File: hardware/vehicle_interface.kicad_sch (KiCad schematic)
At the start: 3 parts, among them J2 FCR7350, J3 FCR7350, J4 FCR7350

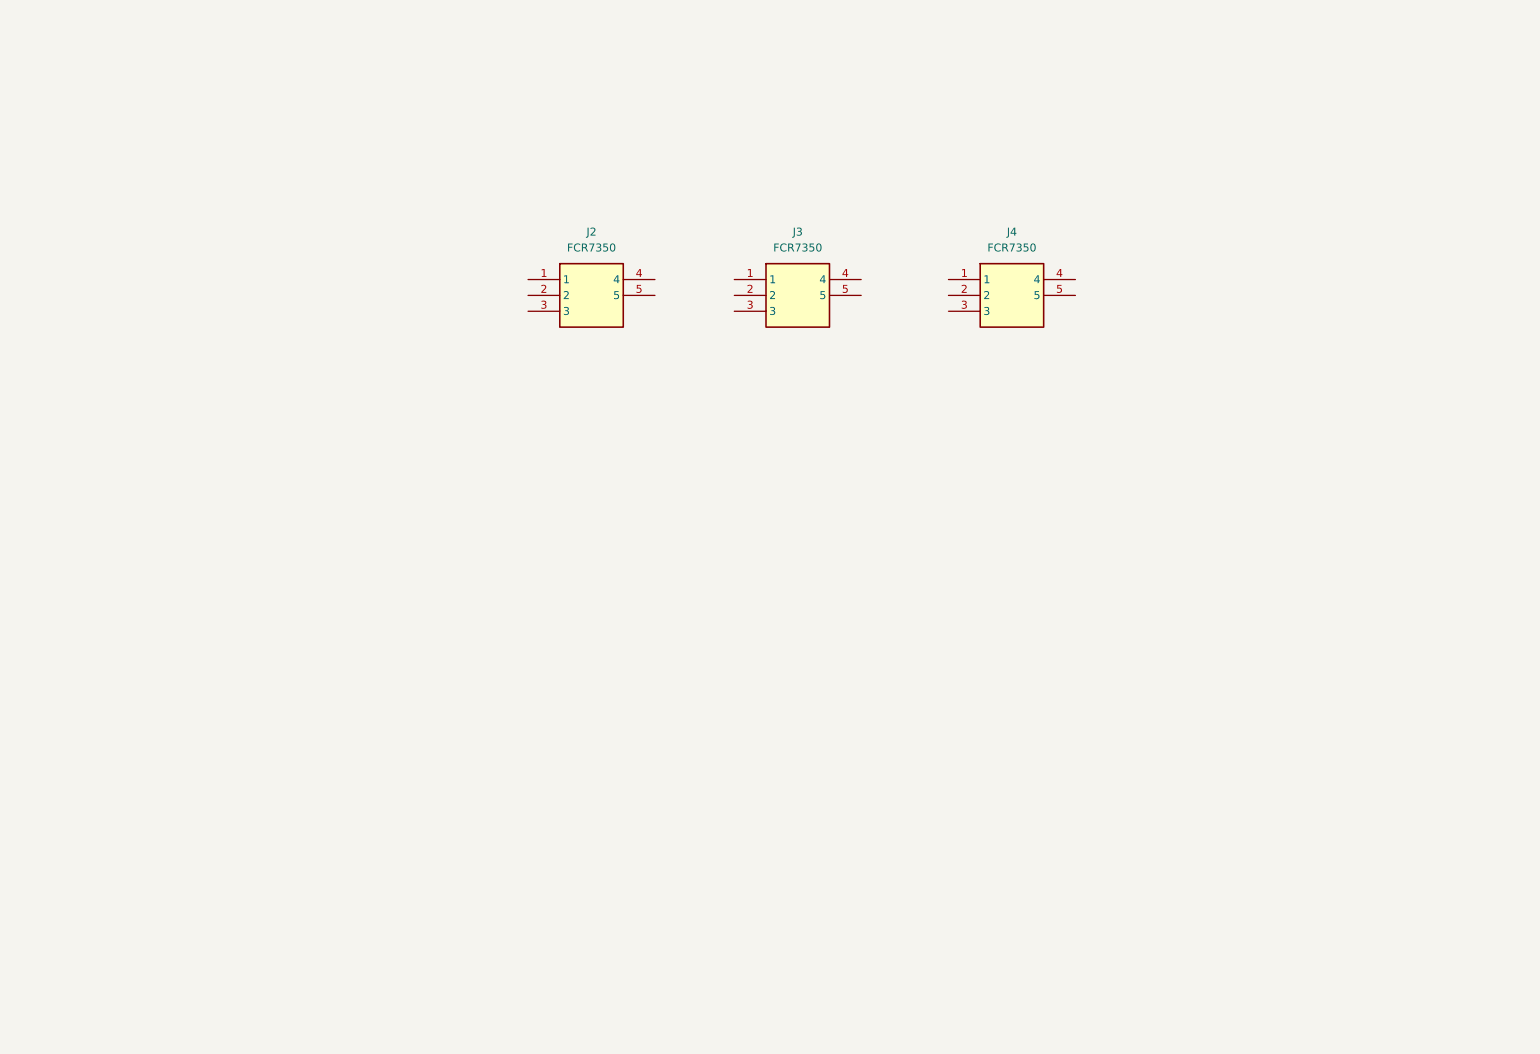
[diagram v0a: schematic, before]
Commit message: CAN ADC on the board
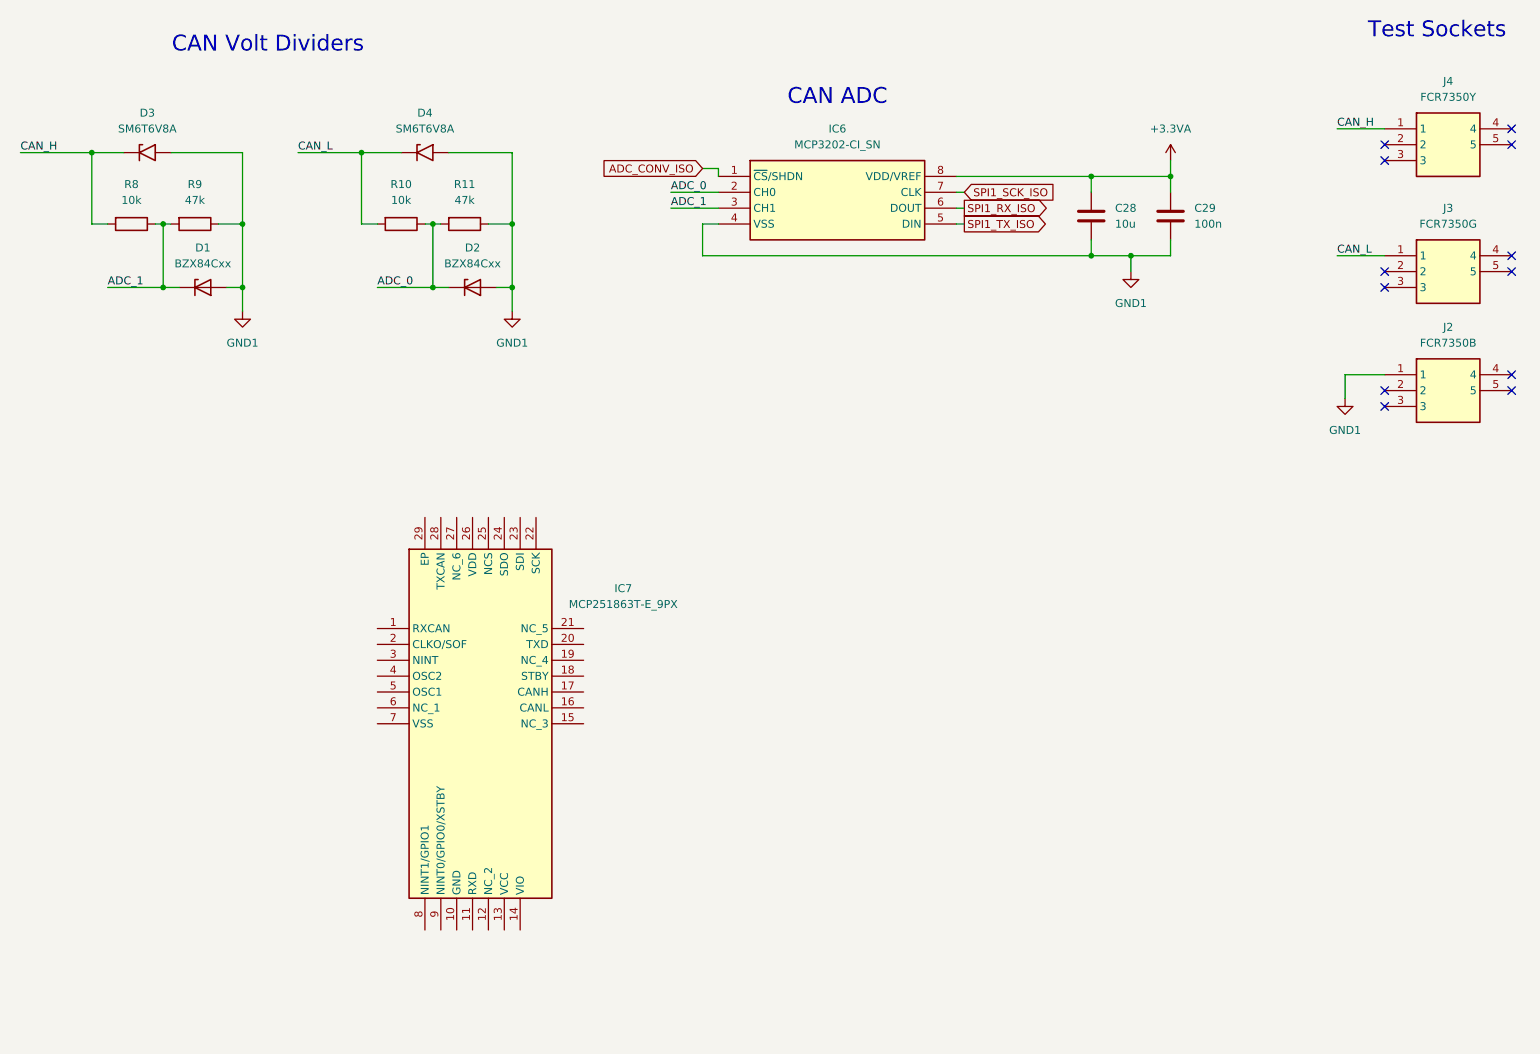
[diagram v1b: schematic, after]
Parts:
- added C28: 10u, Capacitor_SMD:C_0603_1608Metric, symbol Device:C
- added C29: 100n, Capacitor_SMD:C_0402_1005Metric, symbol Device:C
- added D1, D2: BZX84Cxx, Package_TO_SOT_SMD:SOT-23, symbol Diode:BZX84Cxx
- added D3, D4: SM6T6V8A, Diode_SMD:D_SMB, symbol Diode:SM6T6V8A
- added IC6: MCP3202-CI_SN, Stuttgart:SOIC127P600X175-8N, symbol Stuttgart:MCP3202-CI_SN
- added IC7: MCP251863T-E_9PX, Stuttgart:QFN50P500X500X90-29N-D, symbol Stuttgart:MCP251863T-E_9PX
- added R10, R8: 10k, Resistor_SMD:R_0402_1005Metric, symbol Device:R
- added R11, R9: 47k, Resistor_SMD:R_0402_1005Metric, symbol Device:R
- J2: value FCR7350 -> FCR7350B
- J3: value FCR7350 -> FCR7350G
- J4: value FCR7350 -> FCR7350Y
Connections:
- net CAN_H: now reaches J4.1
- net CAN_H: now also D3.1 (A1), R8.2
- net CAN_L: now reaches J3.1
- net CAN_L: now also D4.1 (A1), R10.2
- net GND1: now reaches J2.1
- net GND1: now also C28.2, C29.2, D1.1 (A), D2.1 (A), D3.2 (A2), D4.2 (A2), IC6.4 (VSS), R11.1, R9.1
- new net +3.3VA: C28.1, C29.1, IC6.8 (VDD/VREF)
- new net ADC_0: D2.3 (K), IC6.2 (CH0), R10.1, R11.2
- new net ADC_1: D1.3 (K), IC6.3 (CH1), R8.1, R9.2
- new net ADC_CONV_ISO: IC6.1 (~{CS}/SHDN)
- new net SPI1_RX_ISO: IC6.6 (DOUT)
- new net SPI1_SCK_ISO: IC6.7 (CLK)
- new net SPI1_TX_ISO: IC6.5 (DIN)
- no-connect marks 0 -> 12
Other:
- note added: "CAN ADC"
- note added: "CAN Volt Dividers"
- note added: "Test Sockets"
- moved on the sheet: J2, J3, J4

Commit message: Further CAN IC work before reworking SPI bridges
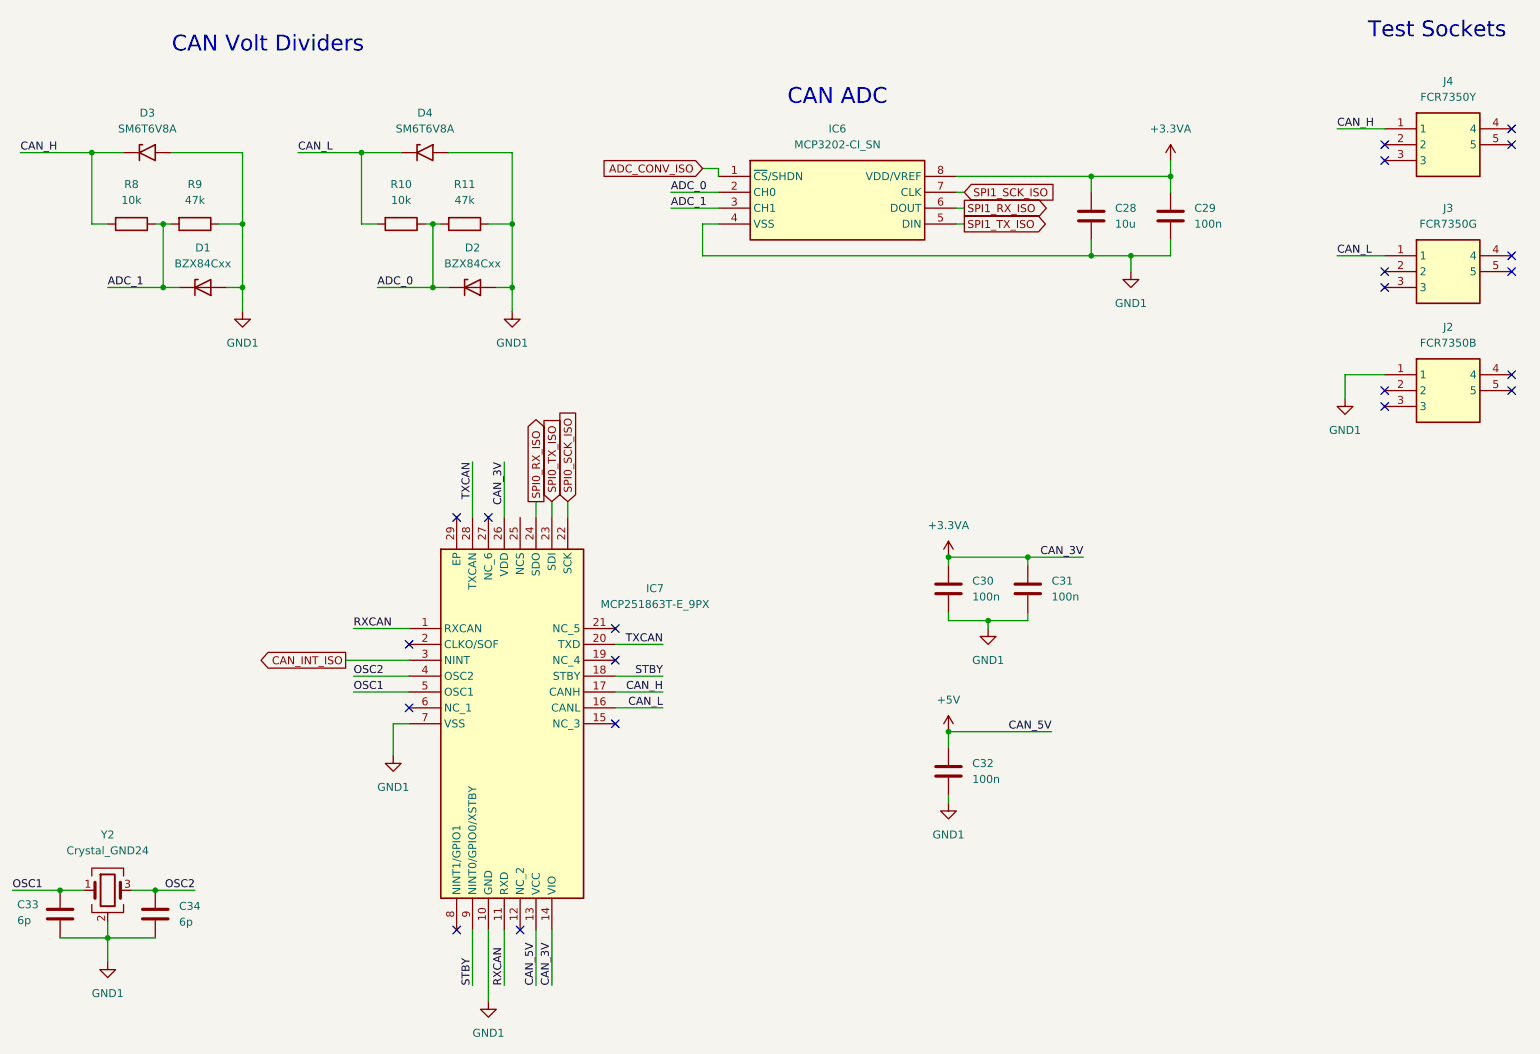
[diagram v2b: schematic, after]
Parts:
- added C30, C31, C32: 100n, Capacitor_SMD:C_0402_1005Metric, symbol Device:C
- added C33, C34: 6p, Capacitor_SMD:C_0402_1005Metric, symbol Device:C
- added Y2: Crystal_GND24, Crystal:Crystal_SMD_2016-4Pin_2.0x1.6mm, symbol Device:Crystal_GND24
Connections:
- net +3.3VA: now also IC7.14 (VIO), IC7.26 (VDD), C30.1, C31.1
- net CAN_H: now also IC7.17 (CANH)
- net CAN_L: now also IC7.16 (CANL)
- net GND1: now also IC7.10 (GND), IC7.7 (VSS), C30.2, C31.2, C32.2, C33.2, C34.2, Y2.2 (G), Y2.4 (G)
- net RXCAN: now reaches IC7.1 (RXCAN)
- net RXCAN: now also IC7.11 (RXD)
- net +5V: now reaches IC7.13 (VCC)
- net +5V: now also C32.1
- net STBY: now reaches IC7.18 (STBY)
- net STBY: now also IC7.9 (NINT0/GPIO0/XSTBY)
- net TXCAN: now reaches IC7.20 (TXD)
- net TXCAN: now also IC7.28 (TXCAN)
- net SPI0_SCK_ISO: now reaches IC7.22 (SCK)
- net SPI0_TX_ISO: now reaches IC7.23 (SDI)
- net SPI0_RX_ISO: now reaches IC7.24 (SDO)
- net CAN_INT_ISO: now reaches IC7.3 (NINT)
- net OSC2: now reaches IC7.4 (OSC2)
- net OSC2: now also C34.1, Y2.3
- net OSC1: now reaches IC7.5 (OSC1)
- net OSC1: now also C33.1, Y2.1
- no-connect marks 12 -> 21
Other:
- moved on the sheet: IC7

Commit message: Further iso bridge development
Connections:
- net SPI0_CS_ISO: now reaches IC7.25 (NCS)
- net CAN_INT1_ISO: now reaches IC7.8 (NINT1/GPIO1)
- net ADC_CONV_ISO renamed SPI1_CS_ISO
- no-connect marks 21 -> 20
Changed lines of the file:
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@@
-	)
-	(no_connect
-		(at 99.06 168.91)
 	)
 	(no_connect
@@
 	(wire
 		(pts
+			(xy 99.06 171.45) (xy 95.25 171.45)
+		)
+		(stroke
+			(width 0)
+			(type default)
+		)
+	)
+	(wire
+		(pts
 			(xy 177.8 137.16) (xy 194.31 137.16)
 		)
@@
 	(wire
 		(pts
+			(xy 99.06 168.91) (xy 99.06 171.45)
+		)
+		(stroke
+			(width 0)
+			(type default)
+		)
+	)
+	(wire
+		(pts
 			(xy 101.6 93.98) (xy 101.6 102.87)
 		)
@@
 		(pts
 			(xy 133.35 53.34) (xy 140.97 53.34)
+		)
+		(stroke
+			(width 0)
+			(type default)
+		)
+	)
+	(wire
+		(pts
+			(xy 109.22 100.33) (xy 109.22 102.87)
 		)
 		(stroke
@@
 		)
 	)
-	(global_label "ADC_CONV_ISO"
+	(global_label "SPI1_CS_ISO"
 		(shape input)
 		(at 138.43 46.99 180)
@@
 		)
 		(property "Intersheetrefs" "${INTERSHEET_REFS}"
-			(at 121.7166 46.99 0)
+			(at 123.5915 46.99 0)
+			(hide yes)
+			(show_name no)
+			(do_not_autoplace no)
+			(effects
+				(font
+					(size 1.27 1.27)
+				)
+				(justify right)
+			)
+		)
+	)
+	(global_label "CAN_INT1_ISO"
+		(shape output)
+		(at 95.25 171.45 180)
+		(fields_autoplaced yes)
+		(effects
+			(font
+				(size 1.27 1.27)
+			)
+			(justify right)
+		)
+		(property "Intersheetrefs" "${INTERSHEET_REFS}"
+			(at 79.3833 171.45 0)
 			(hide yes)
 			(show_name no)
@@
 			(hide yes)
 			(show_name no)
+			(do_not_autoplace no)
+			(effects
+				(font
+					(size 1.27 1.27)
+				)
+				(justify left)
+			)
+		)
+	)
+	(global_label "SPI0_CS_ISO"
+		(shape input)
+		(at 109.22 100.33 90)
+		(fields_autoplaced yes)
+		(effects
+			(font
+				(size 1.27 1.27)
+			)
+			(justify left)
+		)
+		(property "Intersheetrefs" "${INTERSHEET_REFS}"
+			(at 109.22 85.4915 90)
+			(hide yes)
+			(show_name no)

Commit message: Further CAN controller development
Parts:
- C32: footprint Capacitor_SMD:C_0402_1005Metric -> Capacitor_SMD:C_0603_1608Metric
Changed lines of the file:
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@@
+	)
+	(symbol
+		(lib_id "Device:C")
+		(at 177.8 143.51 0)
+		(unit 1)
+		(body_style 1)
+		(exclude_from_sim no)
+		(in_bom yes)
+		(on_board yes)
+		(in_pos_files yes)
+		(dnp no)
+		(fields_autoplaced yes)
+		(property "Reference" "C32"
+			(at 181.61 142.2399 0)
+			(show_name no)
+			(do_not_autoplace no)
+			(effects
+				(font
+					(size 1.27 1.27)
+				)
+				(justify left)
+			)
+		)
+		(property "Value" "100n"
+			(at 181.61 144.7799 0)
+			(show_name no)
+			(do_not_autoplace no)
+			(effects
+				(font
+					(size 1.27 1.27)
+				)
+				(justify left)
+			)
+		)
+		(property "Footprint" "Capacitor_SMD:C_0603_1608Metric"
+			(at 178.7652 147.32 0)
+			(hide yes)
+			(show_name no)
+			(do_not_autoplace no)
+			(effects
+				(font
+					(size 1.27 1.27)
+				)
+			)
+		)
+		(property "Datasheet" ""
+			(at 177.8 143.51 0)
+			(hide yes)
+			(show_name no)
+			(do_not_autoplace no)
+			(effects
+				(font
+					(size 1.27 1.27)
+				)
+			)
+		)
+		(property "Description" "Capacitor, ceramic, 0.1 µF, 50 V,+/- 10%, X7R, 0603"
+			(at 177.8 143.51 0)
+			(hide yes)
+			(show_name no)
+			(do_not_autoplace no)
+			(effects
+				(font
+					(size 1.27 1.27)
+				)
+			)
+		)
+		(pin "2"
+		)
+		(pin "1"
+		)
+		(instances
+			(project "Stuttgart"
+				(path "/6d354744-ce95-4d5c-b7ae-1990dae66f7b/915c1d30-8224-4c06-b75a-21624dbd5336"
+					(reference "C32")
+					(unit 1)
+				)
+			)
+		)
 	)
 	(symbol
@@
 					(unit 1)
 				)
-			)
-		)
-	)
-	(symbol
-		(lib_id "Device:C")
-		(at 177.8 143.51 0)
-		(unit 1)
-		(body_style 1)
-		(exclude_from_sim no)
-		(in_bom yes)
-		(on_board yes)
-		(in_pos_files yes)
-		(dnp no)
-		(fields_autoplaced yes)
-		(property "Reference" "C32"
-			(at 181.61 142.2399 0)
-			(show_name no)
-			(do_not_autoplace no)
-			(effects
-				(font
-					(size 1.27 1.27)
-				)
-				(justify left)
-			)
-		)
-		(property "Value" "100n"
-			(at 181.61 144.7799 0)
-			(show_name no)
-			(do_not_autoplace no)
-			(effects
-				(font
-					(size 1.27 1.27)
-				)
-				(justify left)
-			)
-		)
-		(property "Footprint" "Capacitor_SMD:C_0402_1005Metric"
-			(at 178.7652 147.32 0)
-			(hide yes)
-			(show_name no)
-			(do_not_autoplace no)
-			(effects
-				(font
-					(size 1.27 1.27)
-				)
-			)
-		)
-		(property "Datasheet" ""
-			(at 177.8 143.51 0)
-			(hide yes)
-			(show_name no)
-			(do_not_autoplace no)
-			(effects
-				(font
-					(size 1.27 1.27)
-				)
-			)
-		)
-		(property "Description" "Unpolarized capacitor"
-			(at 177.8 143.51 0)
-			(hide yes)
-			(show_name no)
-			(do_not_autoplace no)
-			(effects
-				(font
-					(size 1.27 1.27)
-				)
-			)
-		)
-		(pin "1"
-		)
-		(pin "2"
-		)
-		(instances
-			(project "Stuttgart"
-				(path "/6d354744-ce95-4d5c-b7ae-1990dae66f7b/915c1d30-8224-4c06-b75a-21624dbd5336"
-					(reference "C32")
-					(unit 1)
-				)

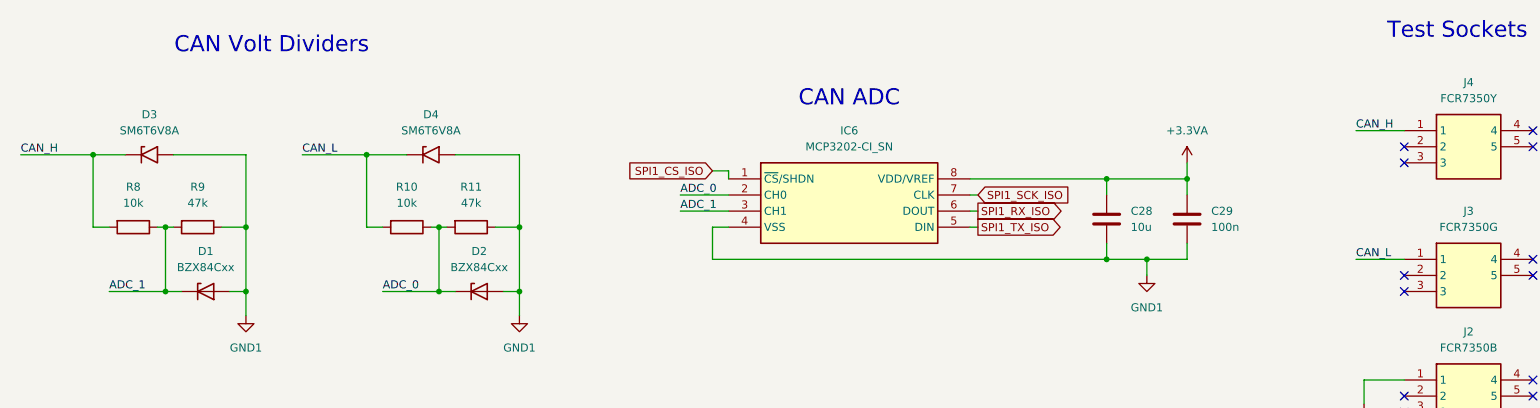
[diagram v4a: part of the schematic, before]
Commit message: Completed ADC, new components and test points
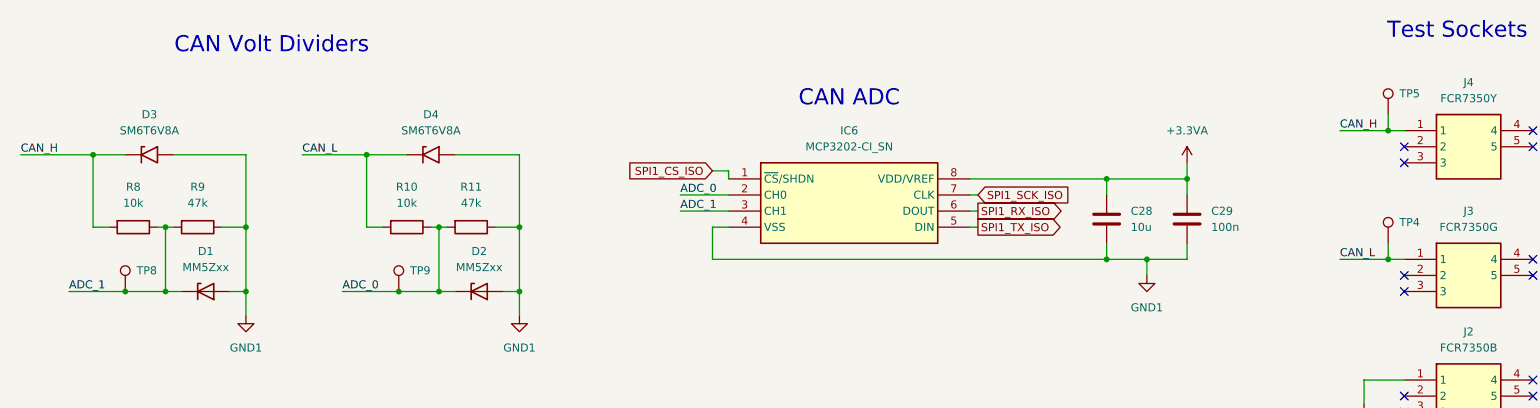
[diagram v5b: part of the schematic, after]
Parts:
- removed D1, D2: BZX84Cxx, Package_TO_SOT_SMD:SOT-23, symbol Diode:BZX84Cxx
- added D1, D2: MM5Zxx, Diode_SMD:D_SOD-523, symbol Diode:MM5Zxx
- added TP4, TP5, TP8, TP9: TestPoint, TestPoint:TestPoint_Pad_D1.0mm, symbol Connector:TestPoint
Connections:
- net ADC_0: now also D2.1 (K), TP9.1
- net ADC_1: now also D1.1 (K), TP8.1
- net CAN_H: now also TP5.1
- net CAN_L: now also TP4.1
- net GND1: now also D1.2 (A), D2.2 (A)
